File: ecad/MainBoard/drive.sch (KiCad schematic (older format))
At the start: 13 parts, among them IC1 RC4558

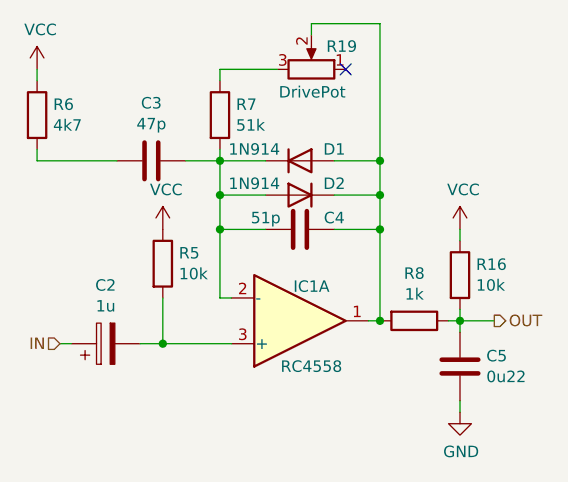
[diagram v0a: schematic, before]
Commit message: Update BOM and SPIRCE SIM
Add netlist to calculate power dissipation through each resistor
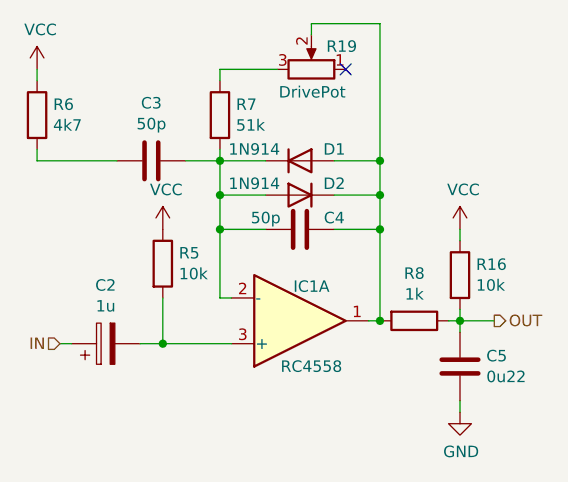
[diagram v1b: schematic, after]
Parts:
- C2: Digi-Key_PN (none) -> 1276-1943-2-ND; MPN (none) -> 1276-1943-2-ND
- C3: value 47p -> 50p; footprint (none) -> Capacitor_SMD:C_0805_2012Metric_Pad1.18x1.45mm_HandSolder; MPN (none) -> GRM0335C1E470JA01D; Spice_Model 47p -> 50p
- C4: value 51p -> 50p; MPN (none) -> GRM0335C1E470JA01D; Spice_Model 51p -> 50p
- C5: MPN (none) -> 885012105011
- D1, D2: Digi-Key_PN (none) -> 1N914MS-ND; MPN (none) -> 1N914
- IC1: Digi-Key_PN (none) -> 296-9650-5-ND; MPN (none) -> RC4558D
- R16, R5: Digi-Key_PN (none) -> RG2012N-474-W-T1; MPN (none) -> RG20N470KWTR-ND
- R6: Digi-Key_PN (none) -> A129546TR-ND; MPN (none) -> CRGH0805F4K7
- R7: Digi-Key_PN (none) -> RMCF1206FT51K0TR-ND; MPN (none) -> RMCF1206FT51K0
- R8: Digi-Key_PN (none) -> A130048TR-ND; MPN (none) -> CRGCQ0402J1K0
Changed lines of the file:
@@
 F 5 "1u" H 850 1900 50  0001 C CNN "Spice_Model"
 F 6 "Y" H 850 1900 50  0001 C CNN "Spice_Netlist_Enabled"
+F 7 "1276-1943-2-ND" H 850 1900 50  0001 C CNN "Digi-Key_PN"
+F 8 "1276-1943-2-ND" H 850 1900 50  0001 C CNN "MPN"
 	1    850  1900
 	0    -1   -1   0
@@
 AR Path="/603069E8/60325725" Ref="C4"  Part="1"
 F 0 "C4" V 1650 1250 50  0000 C CNN
-F 1 "51p" V 1650 1550 50  0000 C CNN
+F 1 "50p" V 1650 1550 50  0000 C CNN
 F 2 "Capacitor_SMD:C_0805_2012Metric_Pad1.18x1.45mm_HandSolder" H 1738 1250 50  0001 C CNN
-F 3 "~" H 1700 1400 50  0001 C CNN
+F 3 "https://search.murata.co.jp/Ceramy/image/img/A01X/G101/ENG/GRM0335C1E470JA01-01.pdf" H 1700 1400 50  0001 C CNN
 F 4 "C" H 1700 1400 50  0001 C CNN "Spice_Primitive"
-F 5 "51p" H 1700 1400 50  0001 C CNN "Spice_Model"
+F 5 "50p" H 1700 1400 50  0001 C CNN "Spice_Model"
 F 6 "Y" H 1700 1400 50  0001 C CNN "Spice_Netlist_Enabled"
+F 7 "GRM0335C1E470JA01D" H 1700 1400 50  0001 C CNN "MPN"
 	1    1700 1400
 	0    -1   1    0
@@
 F 7 "Y" H 1700 1250 50  0001 C CNN "Spice_Netlist_Enabled"
 F 8 "2 1" H 1700 1250 50  0001 C CNN "Spice_Node_Sequence"
+F 9 "1N914MS-ND" H 1700 1250 50  0001 C CNN "Digi-Key_PN"
+F 10 "1N914" H 1700 1250 50  0001 C CNN "MPN"
 	1    1700 1250
 	-1   0    0    -1
@@
 F 7 "../lib/spice_models/1N914.LIB" H 1700 1100 50  0001 C CNN "Spice_Lib_File"
 F 8 "2 1" H 1700 1100 50  0001 C CNN "Spice_Node_Sequence"
+F 9 "1N914MS-ND" H 1700 1100 50  0001 C CNN "Digi-Key_PN"
+F 10 "1N914" H 1700 1100 50  0001 C CNN "MPN"
 	1    1700 1100
 	1    0    0    -1
@@
 F 2 "Resistor_SMD:R_0805_2012Metric_Pad1.20x1.40mm_HandSolder" V 1280 900 50  0001 C CNN
 F 3 "~" H 1350 900 50  0001 C CNN
+F 4 "RMCF1206FT51K0TR-ND" H 1350 900 50  0001 C CNN "Digi-Key_PN"
+F 5 "RMCF1206FT51K0" H 1350 900 50  0001 C CNN "MPN"
 	1    1350 900
 	1    0    0    -1
@@
 F 2 "Resistor_SMD:R_0805_2012Metric_Pad1.20x1.40mm_HandSolder" V 2130 1800 50  0001 C CNN
 F 3 "~" H 2200 1800 50  0001 C CNN
+F 4 "A130048TR-ND" H 2200 1800 50  0001 C CNN "Digi-Key_PN"
+F 5 "CRGCQ0402J1K0" H 2200 1800 50  0001 C CNN "MPN"
 	1    2200 1800
 	0    1    1    0
@@
 F 2 "Resistor_SMD:R_0805_2012Metric_Pad1.20x1.40mm_HandSolder" V 2330 1600 50  0001 C CNN
 F 3 "~" H 2400 1600 50  0001 C CNN
+F 4 "RG2012N-474-W-T1" H 2400 1600 50  0001 C CNN "Digi-Key_PN"
+F 5 "RG20N470KWTR-ND" H 2400 1600 50  0001 C CNN "MPN"
 	1    2400 1600
 	1    0    0    -1
@@
 F 1 "0u22" H 2515 1955 50  0000 L CNN
 F 2 "Capacitor_SMD:C_0805_2012Metric_Pad1.18x1.45mm_HandSolder" H 2438 1850 50  0001 C CNN
-F 3 "~" H 2400 2000 50  0001 C CNN
+F 3 "https://www.we-online.de/katalog/datasheet/885012105011.pdf" H 2400 2000 50  0001 C CNN
 F 4 "C" H 2400 2000 50  0001 C CNN "Spice_Primitive"
 F 5 "0.22u" H 2400 2000 50  0001 C CNN "Spice_Model"
 F 6 "Y" H 2400 2000 50  0001 C CNN "Spice_Netlist_Enabled"
+F 7 "885012105011" H 2400 2000 50  0001 C CNN "MPN"
 	1    2400 2000
 	1    0    0    -1
@@
 F 2 "Resistor_SMD:R_0805_2012Metric_Pad1.20x1.40mm_HandSolder" V 1030 1550 50  0001 C CNN
 F 3 "~" H 1100 1550 50  0001 C CNN
+F 4 "RG2012N-474-W-T1" H 1100 1550 50  0001 C CNN "Digi-Key_PN"
+F 5 "RG20N470KWTR-ND" H 1100 1550 50  0001 C CNN "MPN"
 	1    1100 1550
 	1    0    0    -1
@@
 F 6 "Y" H 1700 1800 50  0001 C CNN "Spice_Netlist_Enabled"
 F 7 "../lib/spice_models/RC4558.301.lib" H 1700 1800 50  0001 C CNN "Spice_Lib_File"
+F 8 "296-9650-5-ND" H 1700 1800 50  0001 C CNN "Digi-Key_PN"
+F 9 "RC4558D" H 1700 1800 50  0001 C CNN "MPN"
 	1    1700 1800
 	1    0    0    1
@@
 P 1050 1100
 F 0 "C3" V 798 1100 50  0000 C CNN
-F 1 "47p" V 889 1100 50  0000 C CNN
-F 2 "" H 1088 950 50  0001 C CNN
-F 3 "~" H 1050 1100 50  0001 C CNN
+F 1 "50p" V 889 1100 50  0000 C CNN
+F 2 "Capacitor_SMD:C_0805_2012Metric_Pad1.18x1.45mm_HandSolder" H 1088 950 50  0001 C CNN
+F 3 "https://search.murata.co.jp/Ceramy/image/img/A01X/G101/ENG/GRM0335C1E470JA01-01.pdf" H 1050 1100 50  0001 C CNN
 F 4 "C" H 1050 1100 50  0001 C CNN "Spice_Primitive"
-F 5 "47p" H 1050 1100 50  0001 C CNN "Spice_Model"
+F 5 "50p" H 1050 1100 50  0001 C CNN "Spice_Model"
 F 6 "Y" H 1050 1100 50  0001 C CNN "Spice_Netlist_Enabled"
+F 7 "GRM0335C1E470JA01D" H 1050 1100 50  0001 C CNN "MPN"
 	1    1050 1100
 	0    1    1    0
@@
 F 5 "4.7k" H 550 900 50  0001 C CNN "Spice_Model"
 F 6 "Y" H 550 900 50  0001 C CNN "Spice_Netlist_Enabled"
+F 7 "A129546TR-ND" H 550 900 50  0001 C CNN "Digi-Key_PN"
+F 8 "CRGH0805F4K7" H 550 900 50  0001 C CNN "MPN"
 	1    550  900
 	1    0    0    -1

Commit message: Corrections + SPICE Model Finally fixed :)
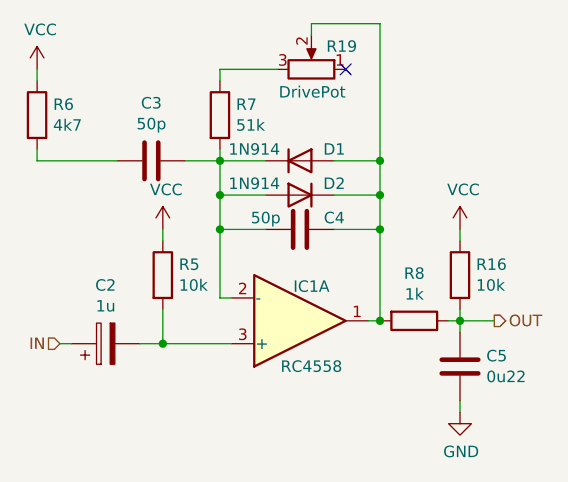
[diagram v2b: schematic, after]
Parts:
- C5: Spice_Model 0.22u -> 0.22uF
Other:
- moved on the sheet: R5
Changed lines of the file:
@@
 F 3 "https://www.we-online.de/katalog/datasheet/885012105011.pdf" H 2400 2000 50  0001 C CNN
 F 4 "C" H 2400 2000 50  0001 C CNN "Spice_Primitive"
-F 5 "0.22u" H 2400 2000 50  0001 C CNN "Spice_Model"
+F 5 "0.22uF" H 2400 2000 50  0001 C CNN "Spice_Model"
 F 6 "Y" H 2400 2000 50  0001 C CNN "Spice_Netlist_Enabled"
 F 7 "885012105011" H 2400 2000 50  0001 C CNN "MPN"
@@
 L Device:R R?
 U 1 1 60325775
-P 1100 1550
+P 1100 1600
 AR Path="/60325775" Ref="R?"  Part="1"
 AR Path="/603069E8/60325775" Ref="R5"  Part="1"
-F 0 "R5" H 1170 1596 50  0000 L CNN
-F 1 "10k" H 1170 1505 50  0000 L CNN
-F 2 "Resistor_SMD:R_0805_2012Metric_Pad1.20x1.40mm_HandSolder" V 1030 1550 50  0001 C CNN
-F 3 "~" H 1100 1550 50  0001 C CNN
-F 4 "RG2012N-474-W-T1" H 1100 1550 50  0001 C CNN "Digi-Key_PN"
-F 5 "RG20N470KWTR-ND" H 1100 1550 50  0001 C CNN "MPN"
-	1    1100 1550
+F 0 "R5" H 1170 1646 50  0000 L CNN
+F 1 "10k" H 1170 1555 50  0000 L CNN
+F 2 "Resistor_SMD:R_0805_2012Metric_Pad1.20x1.40mm_HandSolder" V 1030 1600 50  0001 C CNN
+F 3 "~" H 1100 1600 50  0001 C CNN
+F 4 "RG2012N-474-W-T1" H 1100 1600 50  0001 C CNN "Digi-Key_PN"
+F 5 "RG20N470KWTR-ND" H 1100 1600 50  0001 C CNN "MPN"
+	1    1100 1600
 	1    0    0    -1
 $EndComp
@@
 	1    0    0    -1
 $EndComp
-Wire Wire Line
-	1100 1700 1100 1900
 Connection ~ 1100 1900
 Wire Wire Line
@@
 	2050 500  2050 1100
 Connection ~ 2050 1100
+Wire Wire Line
+	1100 1750 1100 1900
+Wire Wire Line
+	1100 1450 1100 1400
 $EndSCHEMATC

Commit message: Clean up ecad
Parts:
- C2: footprint Capacitor_SMD:C_0805_2012Metric_Pad1.18x1.45mm_HandSolder -> Capacitor_SMD:C_0603_1608Metric_Pad1.08x0.95mm_HandSolder; Digi-Key_PN 1276-1943-2-ND -> 0603ZD106KAT2A; MPN 1276-1943-2-ND -> 0603ZD106KAT2A
- C3, C4: footprint Capacitor_SMD:C_0805_2012Metric_Pad1.18x1.45mm_HandSolder -> Capacitor_SMD:C_0201_0603Metric_Pad0.64x0.40mm_HandSolder; Digi-Key_PN (none) -> 490-1256-6-ND
- C5: footprint Capacitor_SMD:C_0805_2012Metric_Pad1.18x1.45mm_HandSolder -> Capacitor_SMD:C_0402_1005Metric_Pad0.74x0.62mm_HandSolder; Digi-Key_PN (none) -> 732-7488-6-ND
- D1, D2: Spice_Lib_File ../lib/spice_models/1N914.LIB -> ../lib/spice_models/1N914.lib
- IC1: footprint Package_SO:Texas_R-PDSO-G8_EP2.95x4.9mm_Mask2.4x3.1mm -> DigiKey:SOIC-8_W3.9mm
- R19: value DrivePot -> 500ka; Category (none) -> Drive Pot; Digi-Key_PN (none) -> 75160-195-08LF; Spice_Lib_File ../lib/spice_models/pot.lib -> ../lib/spice_models/pots.lib
- R7: footprint Resistor_SMD:R_0805_2012Metric_Pad1.20x1.40mm_HandSolder -> Resistor_SMD:R_1206_3216Metric_Pad1.30x1.75mm_HandSolder
- R8: footprint Resistor_SMD:R_0805_2012Metric_Pad1.20x1.40mm_HandSolder -> Resistor_SMD:R_0402_1005Metric_Pad0.72x0.64mm_HandSolder

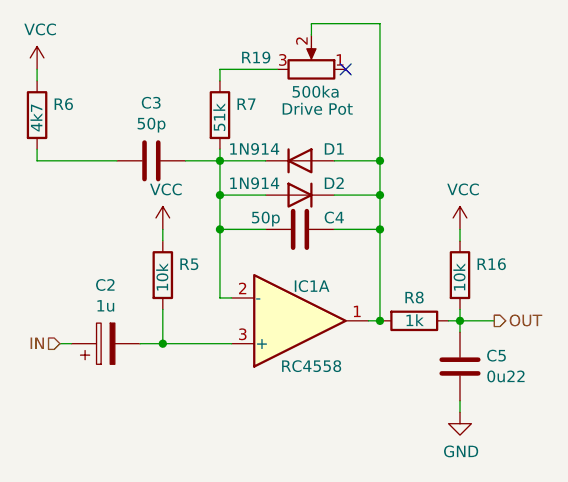
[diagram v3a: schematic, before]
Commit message: Update ecad BOM
Change transistor to 2N4424
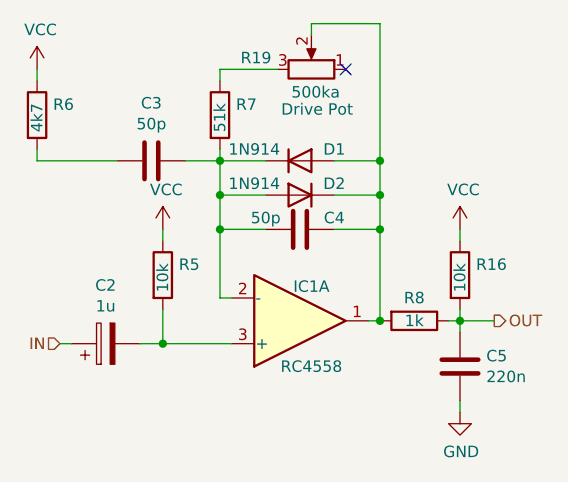
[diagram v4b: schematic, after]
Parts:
- C2: footprint Capacitor_SMD:C_0603_1608Metric_Pad1.08x0.95mm_HandSolder -> Capacitor_SMD:C_0805_2012Metric_Pad1.18x1.45mm_HandSolder; MPN 0603ZD106KAT2A -> C0805C105K4RACTU
- C3, C4: footprint Capacitor_SMD:C_0201_0603Metric_Pad0.64x0.40mm_HandSolder -> Capacitor_SMD:C_0805_2012Metric_Pad1.18x1.45mm_HandSolder; MPN GRM0335C1E470JA01D -> 0805Y0500103KXT
- C5: value 0u22 -> 220n; footprint Capacitor_SMD:C_0402_1005Metric_Pad0.74x0.62mm_HandSolder -> Capacitor_SMD:C_0805_2012Metric_Pad1.18x1.45mm_HandSolder; MPN 885012105011 -> C0805C224K5RACTU
- D1, D2: footprint Diode_THT:D_DO-35_SOD27_P2.54mm_Vertical_AnodeUp -> Diode_THT:D_DO-35_SOD27_P7.62mm_Horizontal
- R16, R5: MPN RG20N470KWTR-ND -> ERJ-6GEYJ103V
- R19: footprint Connector_PinHeader_2.54mm:PinHeader_1x03_P2.54mm_Vertical -> DigiKey:PinHeader_1x3_P2.54_Drill1.1mm; MPN (none) -> 0901200160
- R6: MPN CRGH0805F4K7 -> ERJ-6GEYJ472V
- R7: footprint Resistor_SMD:R_1206_3216Metric_Pad1.30x1.75mm_HandSolder -> Resistor_SMD:R_0805_2012Metric_Pad1.20x1.40mm_HandSolder; MPN RMCF1206FT51K0 -> ERJ-6GEYJ513V
- R8: footprint Resistor_SMD:R_0402_1005Metric_Pad0.72x0.64mm_HandSolder -> Resistor_SMD:R_0805_2012Metric_Pad1.20x1.40mm_HandSolder; MPN CRGCQ0402J1K0 -> ERA6AEB102V
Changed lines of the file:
@@
 F 1 "4k7" V 550 825 50  0000 L CNN
 F 2 "Resistor_SMD:R_0805_2012Metric_Pad1.20x1.40mm_HandSolder" V 480 900 50  0001 C CNN
-F 3 "https://www.te.com/commerce/DocumentDelivery/DDEController?Action=srchrtrv&DocNm=1773204-1&DocType=DS&DocLang=English" H 550 900 50  0001 C CNN
+F 3 "https://datasheet.octopart.com/ERJ-6GEYJ472V-Panasonic-datasheet-13266872.pdf" H 550 900 50  0001 C CNN
 F 4 "R" H 550 900 50  0001 C CNN "Spice_Primitive"
 F 5 "4.7k" H 550 900 50  0001 C CNN "Spice_Model"
 F 6 "Y" H 550 900 50  0001 C CNN "Spice_Netlist_Enabled"
 F 7 "A129546TR-ND" H 550 900 50  0001 C CNN "Digi-Key_PN"
-F 8 "CRGH0805F4K7" H 550 900 50  0001 C CNN "MPN"
+F 8 "ERJ-6GEYJ472V" H 550 900 50  0001 C CNN "MPN"
 	1    550  900
 	1    0    0    -1
@@
 F 0 "C3" V 798 1100 50  0000 C CNN
 F 1 "50p" V 889 1100 50  0000 C CNN
-F 2 "Capacitor_SMD:C_0201_0603Metric_Pad0.64x0.40mm_HandSolder" H 1088 950 50  0001 C CNN
-F 3 "https://search.murata.co.jp/Ceramy/image/img/A01X/G101/ENG/GRM0335C1E470JA01-01.pdf" H 1050 1100 50  0001 C CNN
+F 2 "Capacitor_SMD:C_0805_2012Metric_Pad1.18x1.45mm_HandSolder" H 1088 950 50  0001 C CNN
+F 3 "https://datasheet.octopart.com/0805Y0500103KXT-Syfer-datasheet-8612536.pdf" H 1050 1100 50  0001 C CNN
 F 4 "C" H 1050 1100 50  0001 C CNN "Spice_Primitive"
 F 5 "50p" H 1050 1100 50  0001 C CNN "Spice_Model"
 F 6 "Y" H 1050 1100 50  0001 C CNN "Spice_Netlist_Enabled"
-F 7 "GRM0335C1E470JA01D" H 1050 1100 50  0001 C CNN "MPN"
+F 7 "0805Y0500103KXT" H 1050 1100 50  0001 C CNN "MPN"
 F 8 "490-1256-6-ND" H 1050 1100 50  0001 C CNN "Digi-Key_PN"
 	1    1050 1100
@@
 F 1 "10k" V 1100 1525 50  0000 L CNN
 F 2 "Resistor_SMD:R_0805_2012Metric_Pad1.20x1.40mm_HandSolder" V 1030 1600 50  0001 C CNN
-F 3 "https://www.susumu.co.jp/common/pdf/n_catalog_partition01_en.pdf" H 1100 1600 50  0001 C CNN
+F 3 "https://datasheet.octopart.com/ERJ-6GEYJ103V-Panasonic-datasheet-13266872.pdf" H 1100 1600 50  0001 C CNN
 F 4 "RG2012N-474-W-T1" H 1100 1600 50  0001 C CNN "Digi-Key_PN"
-F 5 "RG20N470KWTR-ND" H 1100 1600 50  0001 C CNN "MPN"
+F 5 "ERJ-6GEYJ103V" H 1100 1600 50  0001 C CNN "MPN"
 	1    1100 1600
 	1    0    0    -1
@@
 AR Path="/603069E8/60325768" Ref="C5"  Part="1"
 F 0 "C5" H 2515 2046 50  0000 L CNN
-F 1 "0u22" H 2515 1955 50  0000 L CNN
-F 2 "Capacitor_SMD:C_0402_1005Metric_Pad0.74x0.62mm_HandSolder" H 2438 1850 50  0001 C CNN
-F 3 "https://www.we-online.de/katalog/datasheet/885012105011.pdf" H 2400 2000 50  0001 C CNN
+F 1 "220n" H 2515 1955 50  0000 L CNN
+F 2 "Capacitor_SMD:C_0805_2012Metric_Pad1.18x1.45mm_HandSolder" H 2438 1850 50  0001 C CNN
+F 3 "https://datasheet.octopart.com/C0805C224K5RACTU-Kemet-datasheet-5313890.pdf" H 2400 2000 50  0001 C CNN
 F 4 "C" H 2400 2000 50  0001 C CNN "Spice_Primitive"
 F 5 "0.22uF" H 2400 2000 50  0001 C CNN "Spice_Model"
 F 6 "Y" H 2400 2000 50  0001 C CNN "Spice_Netlist_Enabled"
-F 7 "885012105011" H 2400 2000 50  0001 C CNN "MPN"
+F 7 "C0805C224K5RACTU" H 2400 2000 50  0001 C CNN "MPN"
 F 8 "732-7488-6-ND" H 2400 2000 50  0001 C CNN "Digi-Key_PN"
 	1    2400 2000
@@
 F 1 "10k" V 2400 1525 50  0000 L CNN
 F 2 "Resistor_SMD:R_0805_2012Metric_Pad1.20x1.40mm_HandSolder" V 2330 1600 50  0001 C CNN
-F 3 "https://www.susumu.co.jp/common/pdf/n_catalog_partition01_en.pdf" H 2400 1600 50  0001 C CNN
+F 3 "https://datasheet.octopart.com/ERJ-6GEYJ103V-Panasonic-datasheet-13266872.pdf" H 2400 1600 50  0001 C CNN
 F 4 "RG2012N-474-W-T1" H 2400 1600 50  0001 C CNN "Digi-Key_PN"
-F 5 "RG20N470KWTR-ND" H 2400 1600 50  0001 C CNN "MPN"
+F 5 "ERJ-6GEYJ103V" H 2400 1600 50  0001 C CNN "MPN"
 	1    2400 1600
 	1    0    0    -1
@@
 F 0 "R8" V 2100 1800 50  0000 C CNN
 F 1 "1k" V 2200 1800 50  0000 C CNN
-F 2 "Resistor_SMD:R_0402_1005Metric_Pad0.72x0.64mm_HandSolder" V 2130 1800 50  0001 C CNN
-F 3 "https://www.te.com/commerce/DocumentDelivery/DDEController?Action=srchrtrv&DocNm=1773204-3&DocType=DS&DocLang=English" H 2200 1800 50  0001 C CNN
+F 2 "Resistor_SMD:R_0805_2012Metric_Pad1.20x1.40mm_HandSolder" V 2130 1800 50  0001 C CNN
+F 3 "https://datasheet.octopart.com/ERA6AEB102V-Panasonic-datasheet-62287448.pdf" H 2200 1800 50  0001 C CNN
 F 4 "A130048TR-ND" H 2200 1800 50  0001 C CNN "Digi-Key_PN"
-F 5 "CRGCQ0402J1K0" H 2200 1800 50  0001 C CNN "MPN"
+F 5 "ERA6AEB102V" H 2200 1800 50  0001 C CNN "MPN"
 	1    2200 1800
 	0    1    1    0
@@
 F 0 "R7" H 1420 946 50  0000 L CNN
 F 1 "51k" V 1350 825 50  0000 L CNN
-F 2 "Resistor_SMD:R_1206_3216Metric_Pad1.30x1.75mm_HandSolder" V 1280 900 50  0001 C CNN
-F 3 "https://www.seielect.com/catalog/sei-rmcf_rmcp.pdf" H 1350 900 50  0001 C CNN
+F 2 "Resistor_SMD:R_0805_2012Metric_Pad1.20x1.40mm_HandSolder" V 1280 900 50  0001 C CNN
+F 3 "https://datasheet.octopart.com/ERJ-6GEYJ513V-Panasonic-datasheet-61114972.pdf" H 1350 900 50  0001 C CNN
 F 4 "RMCF1206FT51K0TR-ND" H 1350 900 50  0001 C CNN "Digi-Key_PN"
-F 5 "RMCF1206FT51K0" H 1350 900 50  0001 C CNN "MPN"
+F 5 "ERJ-6GEYJ513V" H 1350 900 50  0001 C CNN "MPN"
 	1    1350 900
 	1    0    0    -1
@@
 F 0 "D1" H 1850 1150 50  0000 C CNN
 F 1 "1N914" H 1500 1150 50  0000 C CNN
-F 2 "Diode_THT:D_DO-35_SOD27_P2.54mm_Vertical_AnodeUp" H 1700 925 50  0001 C CNN
-F 3 "http://www.vishay.com/docs/85622/1n914.pdf" H 1700 1100 50  0001 C CNN
+F 2 "Diode_THT:D_DO-35_SOD27_P7.62mm_Horizontal" H 1700 925 50  0001 C CNN
+F 3 "https://datasheet.octopart.com/1N914-ON-Semiconductor-datasheet-42765246.pdf" H 1700 1100 50  0001 C CNN
 F 4 "D" H 1700 1100 50  0001 C CNN "Spice_Primitive"
 F 5 "D1N914" H 1700 1100 50  0001 C CNN "Spice_Model"
@@
 F 0 "D2" H 1550 1300 50  0000 C CNN
 F 1 "1N914" H 1900 1300 50  0000 C CNN
-F 2 "Diode_THT:D_DO-35_SOD27_P2.54mm_Vertical_AnodeUp" H 1700 1075 50  0001 C CNN
-F 3 "http://www.vishay.com/docs/85622/1n914.pdf" H 1700 1250 50  0001 C CNN
+F 2 "Diode_THT:D_DO-35_SOD27_P7.62mm_Horizontal" H 1700 1075 50  0001 C CNN
+F 3 "https://datasheet.octopart.com/1N914-ON-Semiconductor-datasheet-42765246.pdf" H 1700 1250 50  0001 C CNN
 F 4 "../lib/spice_models/1N914.lib" H 1700 1250 50  0001 C CNN "Spice_Lib_File"
 F 5 "D" H 1700 1250 50  0001 C CNN "Spice_Primitive"
@@
 F 0 "C4" V 1650 1250 50  0000 C CNN
 F 1 "50p" V 1650 1550 50  0000 C CNN
-F 2 "Capacitor_SMD:C_0201_0603Metric_Pad0.64x0.40mm_HandSolder" H 1738 1250 50  0001 C CNN
-F 3 "https://search.murata.co.jp/Ceramy/image/img/A01X/G101/ENG/GRM0335C1E470JA01-01.pdf" H 1700 1400 50  0001 C CNN
+F 2 "Capacitor_SMD:C_0805_2012Metric_Pad1.18x1.45mm_HandSolder" H 1738 1250 50  0001 C CNN
+F 3 "https://datasheet.octopart.com/0805Y0500103KXT-Syfer-datasheet-8612536.pdf" H 1700 1400 50  0001 C CNN
 F 4 "C" H 1700 1400 50  0001 C CNN "Spice_Primitive"
 F 5 "50p" H 1700 1400 50  0001 C CNN "Spice_Model"
 F 6 "Y" H 1700 1400 50  0001 C CNN "Spice_Netlist_Enabled"
-F 7 "GRM0335C1E470JA01D" H 1700 1400 50  0001 C CNN "MPN"
+F 7 "0805Y0500103KXT" H 1700 1400 50  0001 C CNN "MPN"
 F 8 "490-1256-6-ND" H 1700 1400 50  0001 C CNN "Digi-Key_PN"
 	1    1700 1400
@@
 F 0 "C2" V 1105 1900 50  0000 C CNN
 F 1 "1u" V 1014 1900 50  0000 C CNN
-F 2 "Capacitor_SMD:C_0603_1608Metric_Pad1.08x0.95mm_HandSolder" H 888 1750 50  0001 C CNN
-F 3 "https://datasheets.avx.com/cx5r.pdf" H 850 1900 50  0001 C CNN
+F 2 "Capacitor_SMD:C_0805_2012Metric_Pad1.18x1.45mm_HandSolder" H 888 1750 50  0001 C CNN
+F 3 "https://datasheet.octopart.com/C0805C105K4RACTU-KEMET-datasheet-149523919.pdf" H 850 1900 50  0001 C CNN
 F 4 "C" H 850 1900 50  0001 C CNN "Spice_Primitive"
 F 5 "1u" H 850 1900 50  0001 C CNN "Spice_Model"
 F 6 "Y" H 850 1900 50  0001 C CNN "Spice_Netlist_Enabled"
 F 7 "0603ZD106KAT2A" H 850 1900 50  0001 C CNN "Digi-Key_PN"
-F 8 "0603ZD106KAT2A" H 850 1900 50  0001 C CNN "MPN"
+F 8 "C0805C105K4RACTU" H 850 1900 50  0001 C CNN "MPN"
 	1    850  1900
 	0    -1   -1   0
@@
 F 0 "R19" V 1800 525 50  0000 R CNN
 F 1 "500ka" V 1650 825 50  0000 R CNN
-F 2 "Connector_PinHeader_2.54mm:PinHeader_1x03_P2.54mm_Vertical" H 1750 700 50  0001 C CNN
-F 3 "https://www.bourns.com/docs/Product-Datasheets/PTV09.pdf" H 1750 700 50  0001 C CNN
+F 2 "DigiKey:PinHeader_1x3_P2.54_Drill1.1mm" H 1750 700 50  0001 C CNN
+F 3 "https://www.molex.com/pdm_docs/sd/901200160_sd.pdf" H 1750 700 50  0001 C CNN
 F 4 "X" H 1750 700 50  0001 C CNN "Spice_Primitive"
 F 5 "POTDrive" H 1750 700 50  0001 C CNN "Spice_Model"
@@
 F 8 "Drive Pot" V 1575 725 50  0000 C CNN "Category"
 F 9 "75160-195-08LF" H 1750 700 50  0001 C CNN "Digi-Key_PN"
-F 10 "" H 1750 700 50  0001 C CNN "MPN"
+F 10 "0901200160" H 1750 700 50  0001 C CNN "MPN"
 	1    1750 700
 	0    1    -1   0

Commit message: Library recovery
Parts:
- D1, D2: footprint Diode_THT:D_DO-35_SOD27_P7.62mm_Horizontal -> Diode_THT:D_DO-35_SOD27_P5.08mm_Vertical_KathodeUp
- IC1: footprint DigiKey:SOIC-8_W3.9mm -> digikey-footprints:SOIC-8_W5.6mm
- R19: footprint DigiKey:PinHeader_1x3_P2.54_Drill1.1mm -> screaming-panda:75160-195-03LF
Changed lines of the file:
@@
 F 0 "IC1" H 1750 1650 50  0000 C CNN
 F 1 "RC4558" H 1750 2000 50  0000 C CNN
-F 2 "DigiKey:SOIC-8_W3.9mm" H 1700 1800 50  0001 C CNN
+F 2 "digikey-footprints:SOIC-8_W5.6mm" H 1700 1800 50  0001 C CNN
 F 3 "http://www.ti.com/lit/ds/symlink/rc4558.pdf" H 1700 1800 50  0001 C CNN
 F 4 "X" H 1700 1800 50  0001 C CNN "Spice_Primitive"
@@
 F 0 "D1" H 1850 1150 50  0000 C CNN
 F 1 "1N914" H 1500 1150 50  0000 C CNN
-F 2 "Diode_THT:D_DO-35_SOD27_P7.62mm_Horizontal" H 1700 925 50  0001 C CNN
+F 2 "Diode_THT:D_DO-35_SOD27_P5.08mm_Vertical_KathodeUp" H 1700 925 50  0001 C CNN
 F 3 "https://datasheet.octopart.com/1N914-ON-Semiconductor-datasheet-42765246.pdf" H 1700 1100 50  0001 C CNN
 F 4 "D" H 1700 1100 50  0001 C CNN "Spice_Primitive"
@@
 F 0 "D2" H 1550 1300 50  0000 C CNN
 F 1 "1N914" H 1900 1300 50  0000 C CNN
-F 2 "Diode_THT:D_DO-35_SOD27_P7.62mm_Horizontal" H 1700 1075 50  0001 C CNN
+F 2 "Diode_THT:D_DO-35_SOD27_P5.08mm_Vertical_KathodeUp" H 1700 1075 50  0001 C CNN
 F 3 "https://datasheet.octopart.com/1N914-ON-Semiconductor-datasheet-42765246.pdf" H 1700 1250 50  0001 C CNN
 F 4 "../lib/spice_models/1N914.lib" H 1700 1250 50  0001 C CNN "Spice_Lib_File"
@@
 F 0 "R19" V 1800 525 50  0000 R CNN
 F 1 "500ka" V 1650 825 50  0000 R CNN
-F 2 "DigiKey:PinHeader_1x3_P2.54_Drill1.1mm" H 1750 700 50  0001 C CNN
+F 2 "screaming-panda:75160-195-03LF" H 1750 700 50  0001 C CNN
 F 3 "https://www.molex.com/pdm_docs/sd/901200160_sd.pdf" H 1750 700 50  0001 C CNN
 F 4 "X" H 1750 700 50  0001 C CNN "Spice_Primitive"
